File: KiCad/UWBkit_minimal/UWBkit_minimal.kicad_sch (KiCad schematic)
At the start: 42 parts, among them J1 Conn_SWD, J2 Conn_BATT, J3 Conn_UART, J7 USB_C_Receptacle_USB2.0_14P, Q1 BSS341, Q2 BSS138, Q3 BSS138, SW1 SW_Push, U2 MAX40203AUK+T, U3 DWM3001C, U4 XC9285B33CMR-G, U6 IP4234CZ6

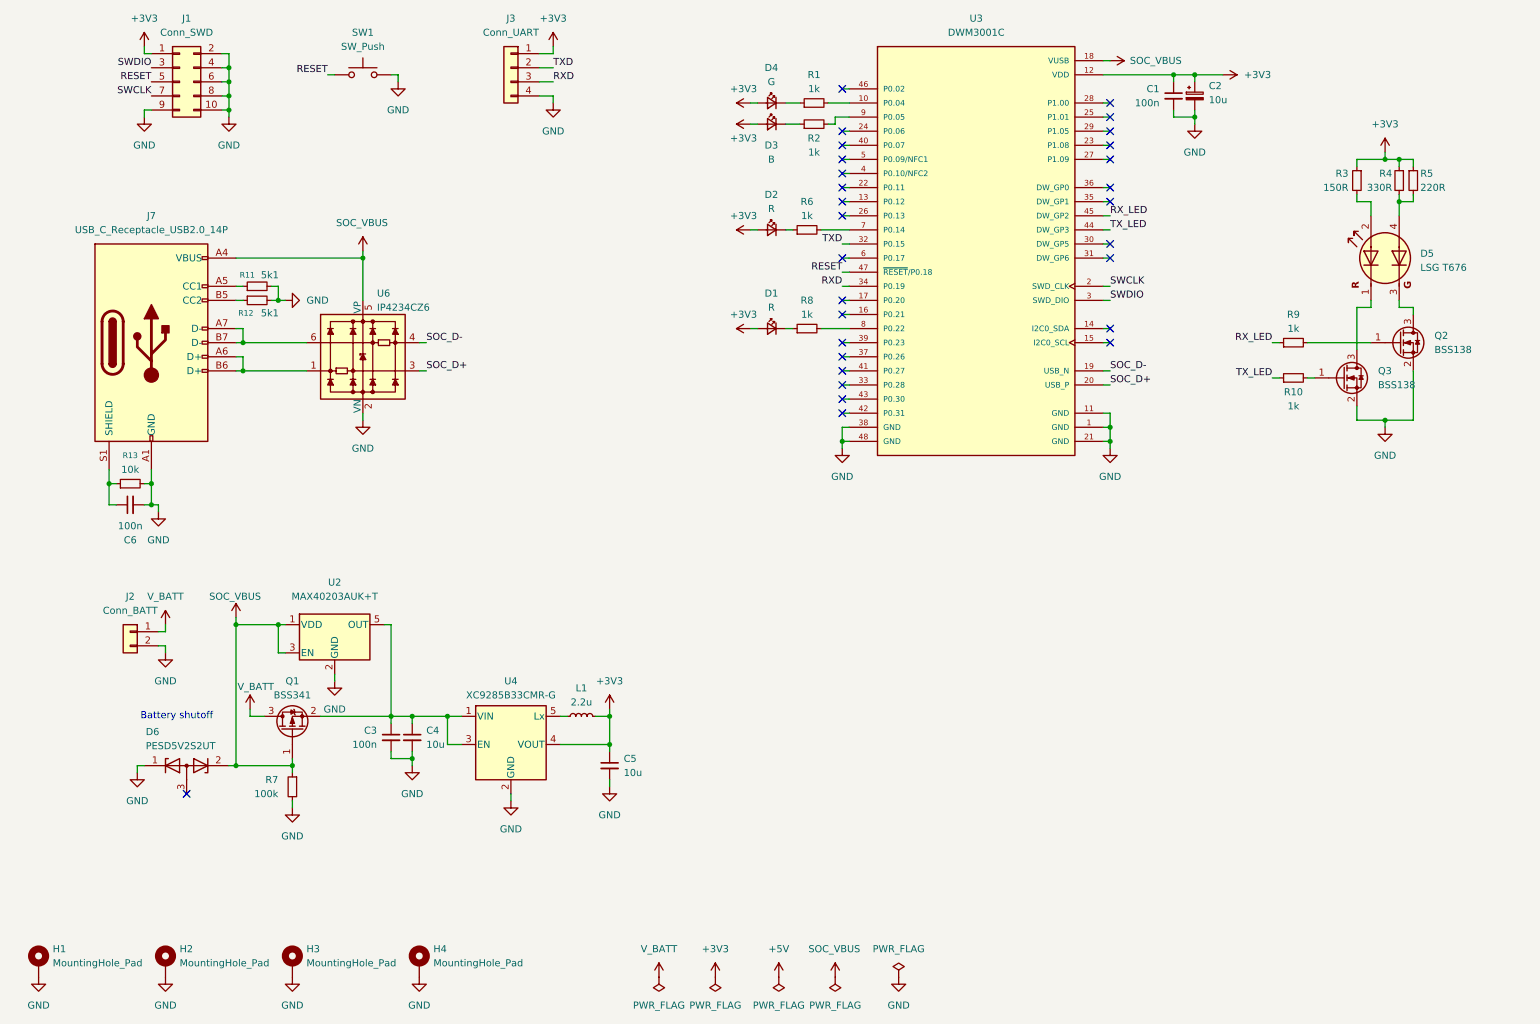
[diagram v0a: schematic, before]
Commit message: Added power led, test points, modified layout
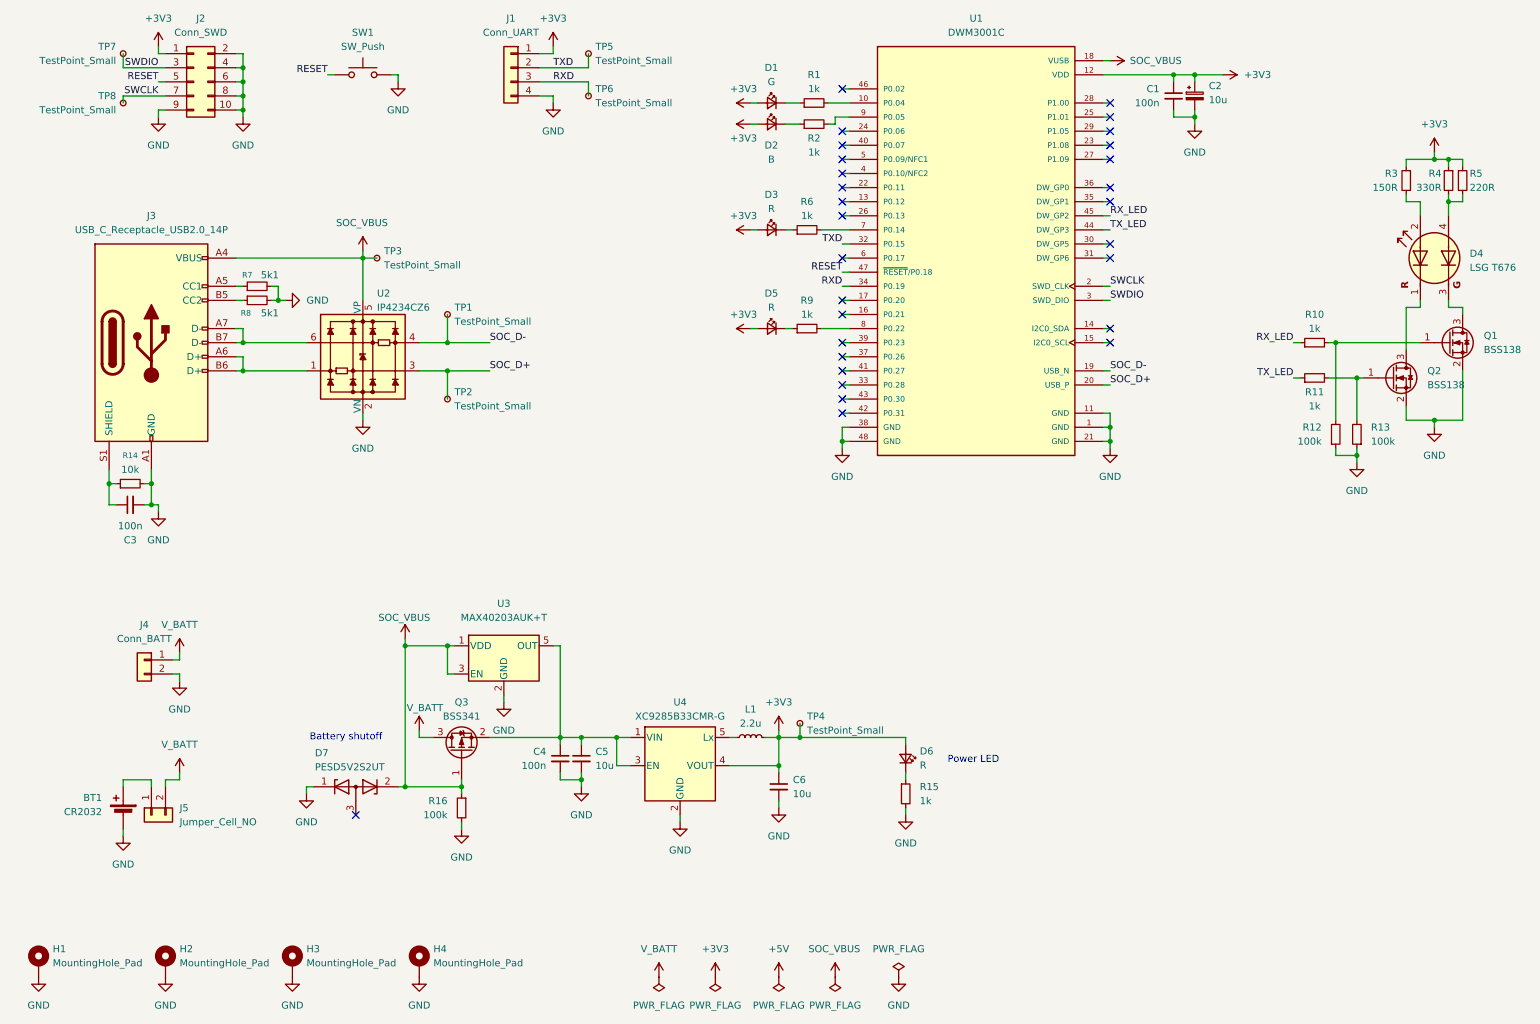
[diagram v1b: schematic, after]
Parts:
- added BT1: CR2032, Battery:BatteryHolder_Keystone_1058_1x2032, symbol Device:Battery_Cell
- added D6: R, LED_SMD:LED_0603_1608Metric, symbol Device:LED_Small
- added J5: Jumper_Cell_NO, Connector_PinHeader_2.54mm:PinHeader_1x02_P2.54mm_Vertical, symbol Connector_Generic:Conn_01x02
- added R12, R13: 100k, Resistor_SMD:R_0603_1608Metric, symbol Device:R_Small
- added R15: 1k, Resistor_SMD:R_0603_1608Metric, symbol Device:R_Small
- added TP1, TP2, TP3, TP4, TP5, TP6, TP7, TP8: TestPoint_Small, TestPoint:TestPoint_Pad_D1.0mm, symbol Connector:TestPoint_Small
- J1: renamed from J3; footprint Connector_PinSocket_2.54mm:PinSocket_1x04_P2.54mm_Vertical_SMD_Pin1Right -> Connector_PinSocket_2.54mm:PinSocket_1x04_P2.54mm_Vertical
- renumbered C6 to C3, C3 to C4, C4 to C5, C5 to C6, D4 to D1, D3 to D2, D2 to D3, D5 to D4, D1 to D5, D6 to D7, J1 to J2, J7 to J3, J2 to J4, Q2 to Q1, Q3 to Q2, Q1 to Q3, R9 to R10, R10 to R11, R13 to R14, R7 to R16, R11 to R7, R12 to R8, R8 to R9, U3 to U1, U6 to U2, U2 to U3
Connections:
- net +3V3: now also D6.2 (A), TP4.1
- net GND: now also BT1.2 (-), R12.1, R13.1, R15.2
- net RXD: now also TP6.1
- net SOC_D+: now also TP2.1
- net SOC_D-: now also TP1.1
- net SOC_VBUS: now also TP3.1
- net SWCLK: now also TP8.1
- net SWDIO: now also TP7.1
- net TXD: now also TP5.1
- net V_BATT: now also J5.2 (Pin_2)
- net at Q2.1 (G), R11.2: now also R13.2
- net at Q1.1 (G), R10.2: now also R12.2
- new net: BT1.1 (+), J5.1 (Pin_1)
- new net: D6.1 (K), R15.1
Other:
- note added: "Power LED"
- moved on the sheet: C4, C5, C6, D4, D7, J2, J4, L1, Q1, Q2, Q3, R10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

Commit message: Minor additions
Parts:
- J3: Link (none) -> mouser.com/ProductDetail/GCT/USB4105-GF-A-060?qs=QNEnbhJQKv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
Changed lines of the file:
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@@
+			)
+		)
+		(property "Link" "mouser.com/ProductDetail/GCT/USB4105-GF-A-060?qs=QNEnbhJQKvY2mocwNJzgfA%3D%3D"
+			(at 35.56 74.93 0)
+			(effects
+				(font
+					(size 1.27 1.27)
+				)
+				(hide yes)
 			)
 		)

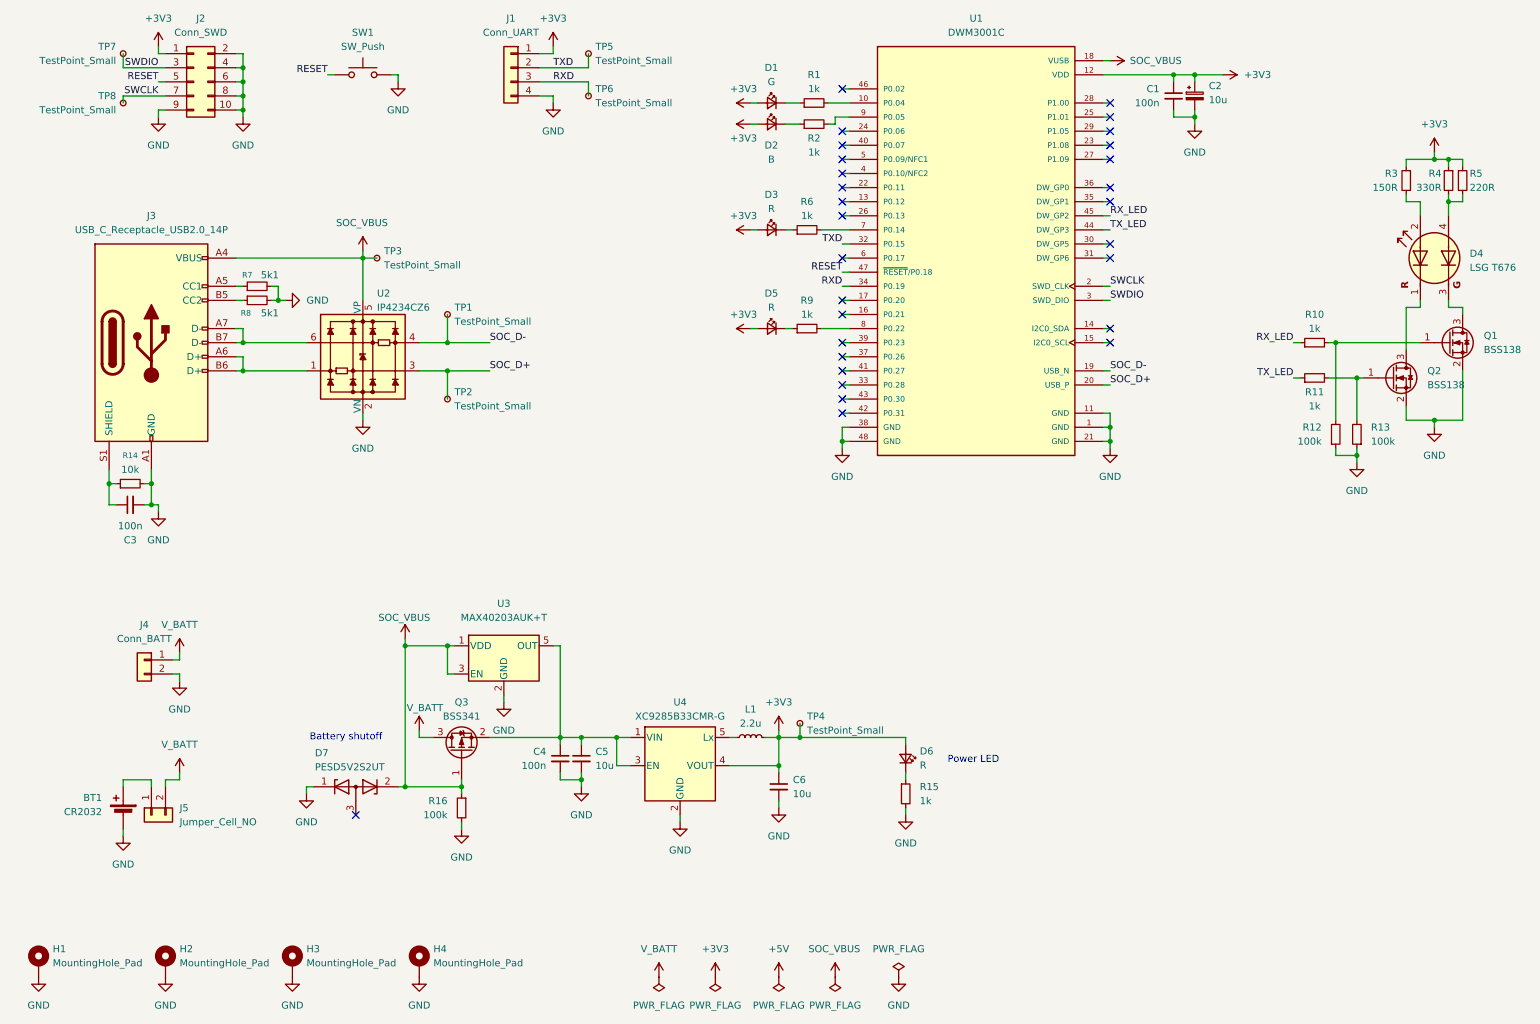
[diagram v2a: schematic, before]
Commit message: Minor changes, added a footprint with QR code
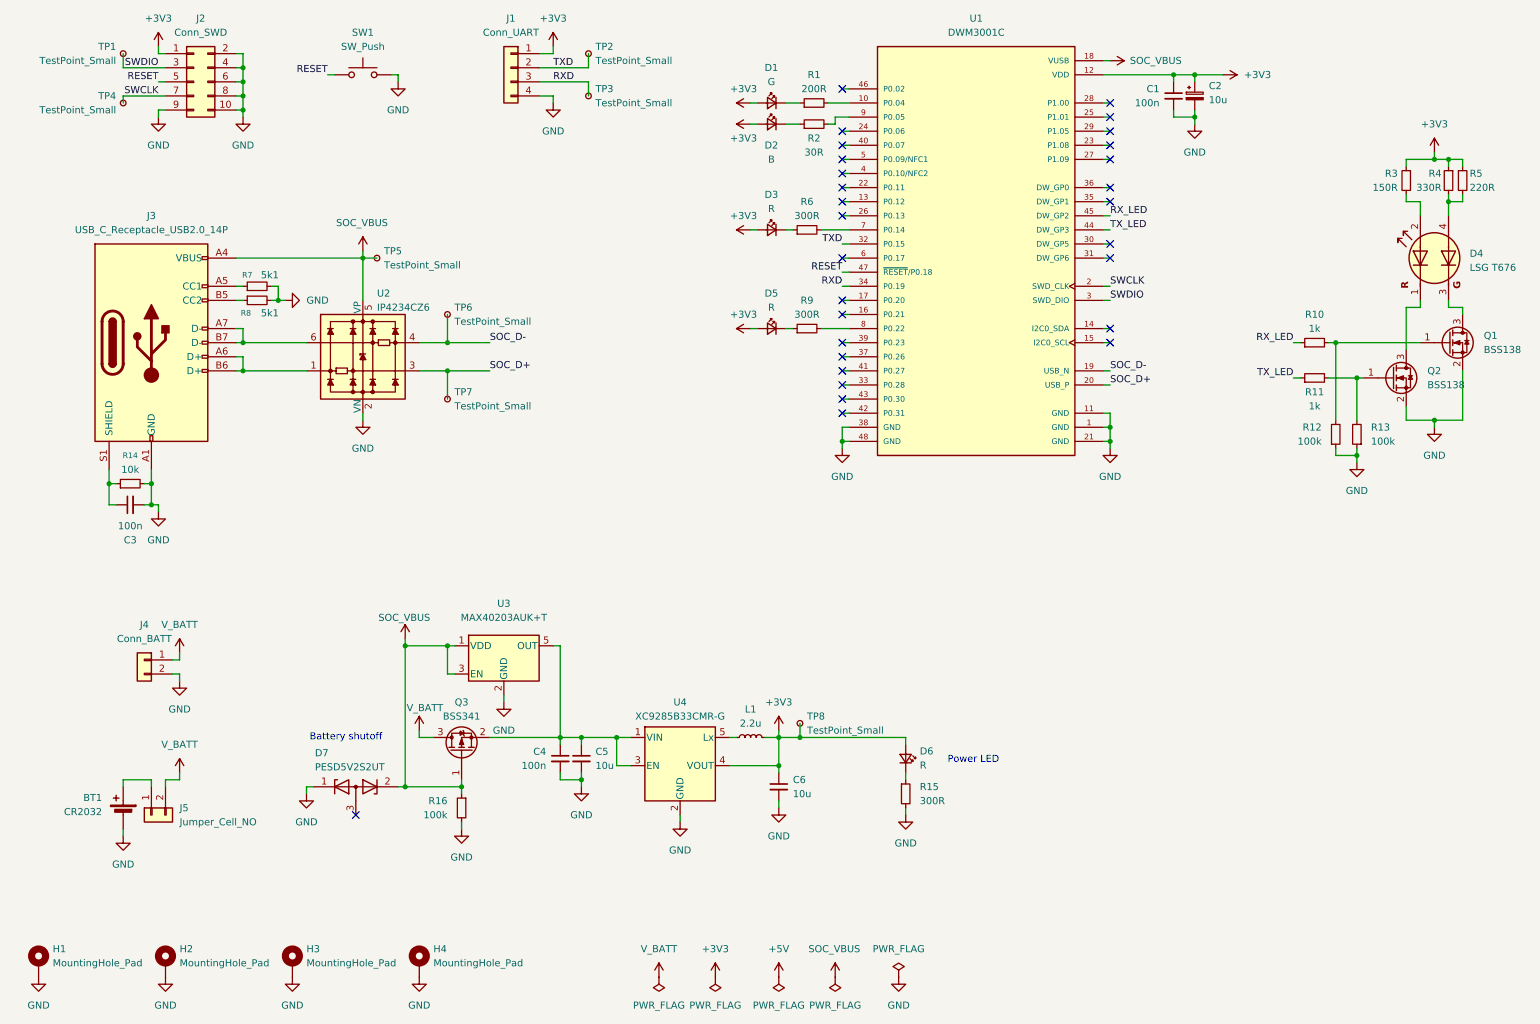
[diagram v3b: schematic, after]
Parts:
- D1: Current (none) -> 2 mA; Mfr No (none) -> 150060GS83000
- D2: Current (none) -> 7 mA; Mfr No (none) -> 150060BS83000
- D3, D5, D6: Current (none) -> 5 mA; Mfr No (none) -> 150060RS83000
- R1: value 1k -> 200R
- R15, R6, R9: value 1k -> 300R
- R2: value 1k -> 30R
- renumbered TP7 to TP1, TP5 to TP2, TP6 to TP3, TP8 to TP4, TP3 to TP5, TP1 to TP6, TP2 to TP7, TP4 to TP8

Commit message: Generated BOM
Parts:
- D4: value LSG T676 -> LSG T676-P7R-1-0+N7P9-24
- Q3: value BSS341 -> BSS84
- TP1, TP2, TP3, TP4, TP5, TP6, TP7, TP8: now left out of the parts list
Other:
- moved on the sheet: BT1, C3, C4, C5, C6, D4, D6, D7, J3, J4, J5, L1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

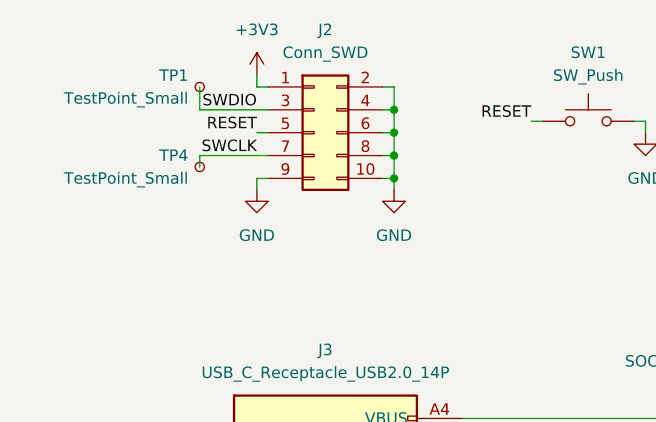
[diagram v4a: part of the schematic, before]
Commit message: Updated pinout for SWD connector
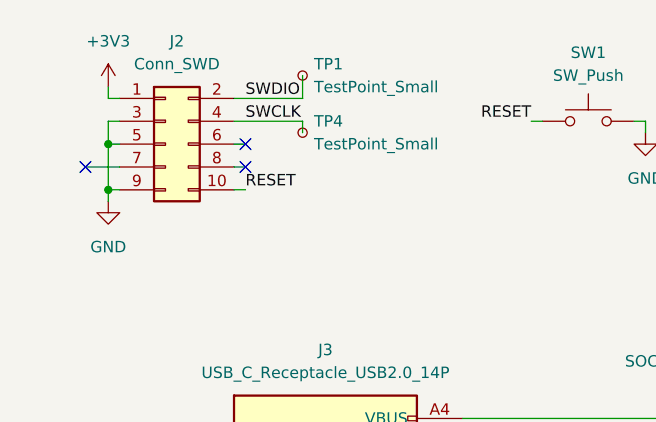
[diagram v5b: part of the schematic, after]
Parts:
- TP1, TP4: footprint TestPoint:TestPoint_Pad_D1.0mm -> TestPoint:TestPoint_Pad_D1.5mm
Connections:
- net GND: now also J2.3 (Pin_3), J2.5 (Pin_5); no longer J2.10 (Pin_10), J2.2 (Pin_2), J2.4 (Pin_4), J2.6 (Pin_6), J2.8 (Pin_8)
- net RESET: now also J2.10 (Pin_10); no longer J2.5 (Pin_5)
- net SWCLK: now also J2.4 (Pin_4); no longer J2.7 (Pin_7)
- net SWDIO: now also J2.2 (Pin_2); no longer J2.3 (Pin_3)
- no-connect marks 29 -> 32
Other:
- moved on the sheet: J2, TP1, TP4

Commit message: PDF export
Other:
- title: (none) -> UWBkit - minimal
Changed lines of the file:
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@@
 	(generator_version "9.0")
 	(paper "A4")
+	(title_block
+		(title "UWBkit - minimal")
+		(date "2025-12-15")
+		(rev "1")
+	)
 	(text "Battery shutoff"
 		(exclude_from_sim no)

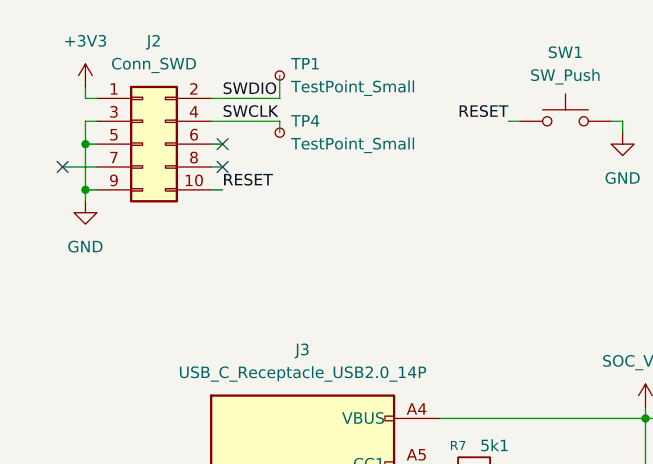
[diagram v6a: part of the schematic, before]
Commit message: Fixed a missing connection to JTAG
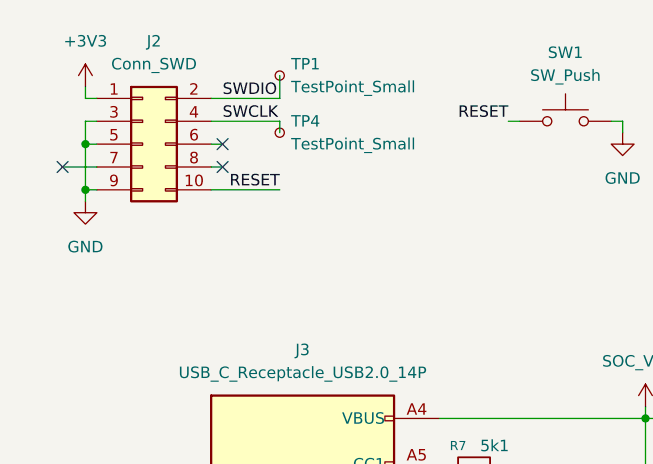
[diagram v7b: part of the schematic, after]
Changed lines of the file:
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@@
 	(wire
 		(pts
-			(xy 35.56 34.29) (xy 34.29 34.29)
+			(xy 41.91 34.29) (xy 34.29 34.29)
 		)
 		(stroke
@@
 	)
 	(label "RESET"
-		(at 35.56 34.29 0)
+		(at 41.91 34.29 180)
 		(effects
 			(font
 				(size 1.27 1.27)
 			)
-			(justify left bottom)
-		)
-	)
+			(justify right bottom)
+		)
+	)
